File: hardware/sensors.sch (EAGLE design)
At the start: 30 parts, among them J1 CDH, J2 OW, J3 DBG, J4 SUN-UART, J5 ADCS, J6 ENV, J7 SUN, U1 DS18B20, U2 DS18B20, U3 DS18B20

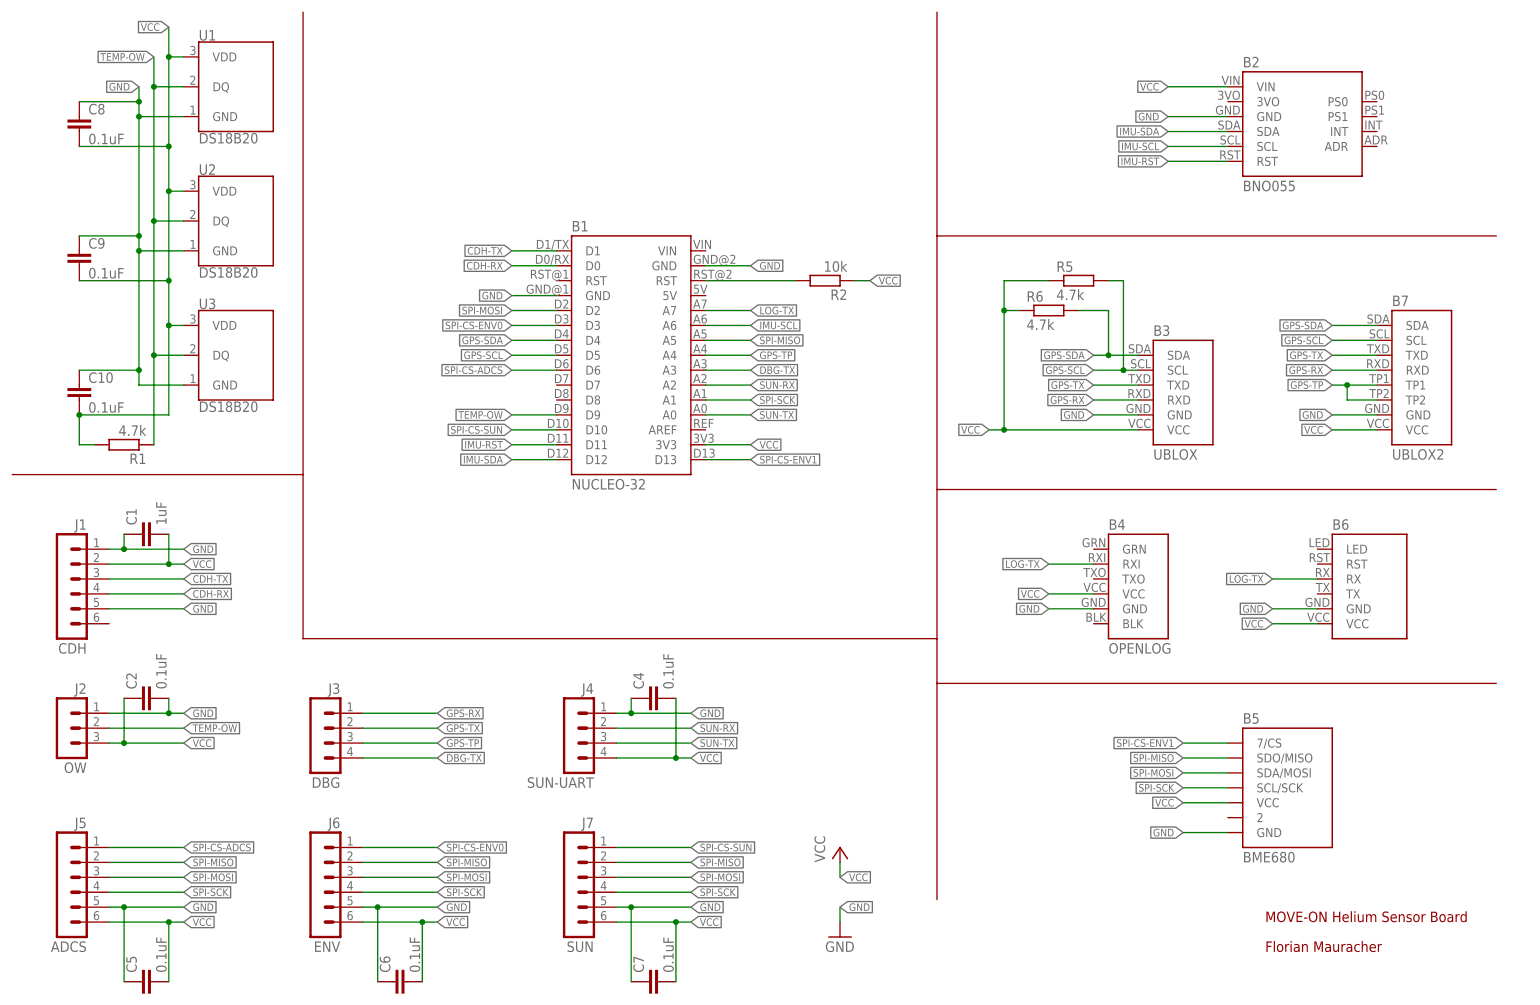
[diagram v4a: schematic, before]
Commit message: Update component names
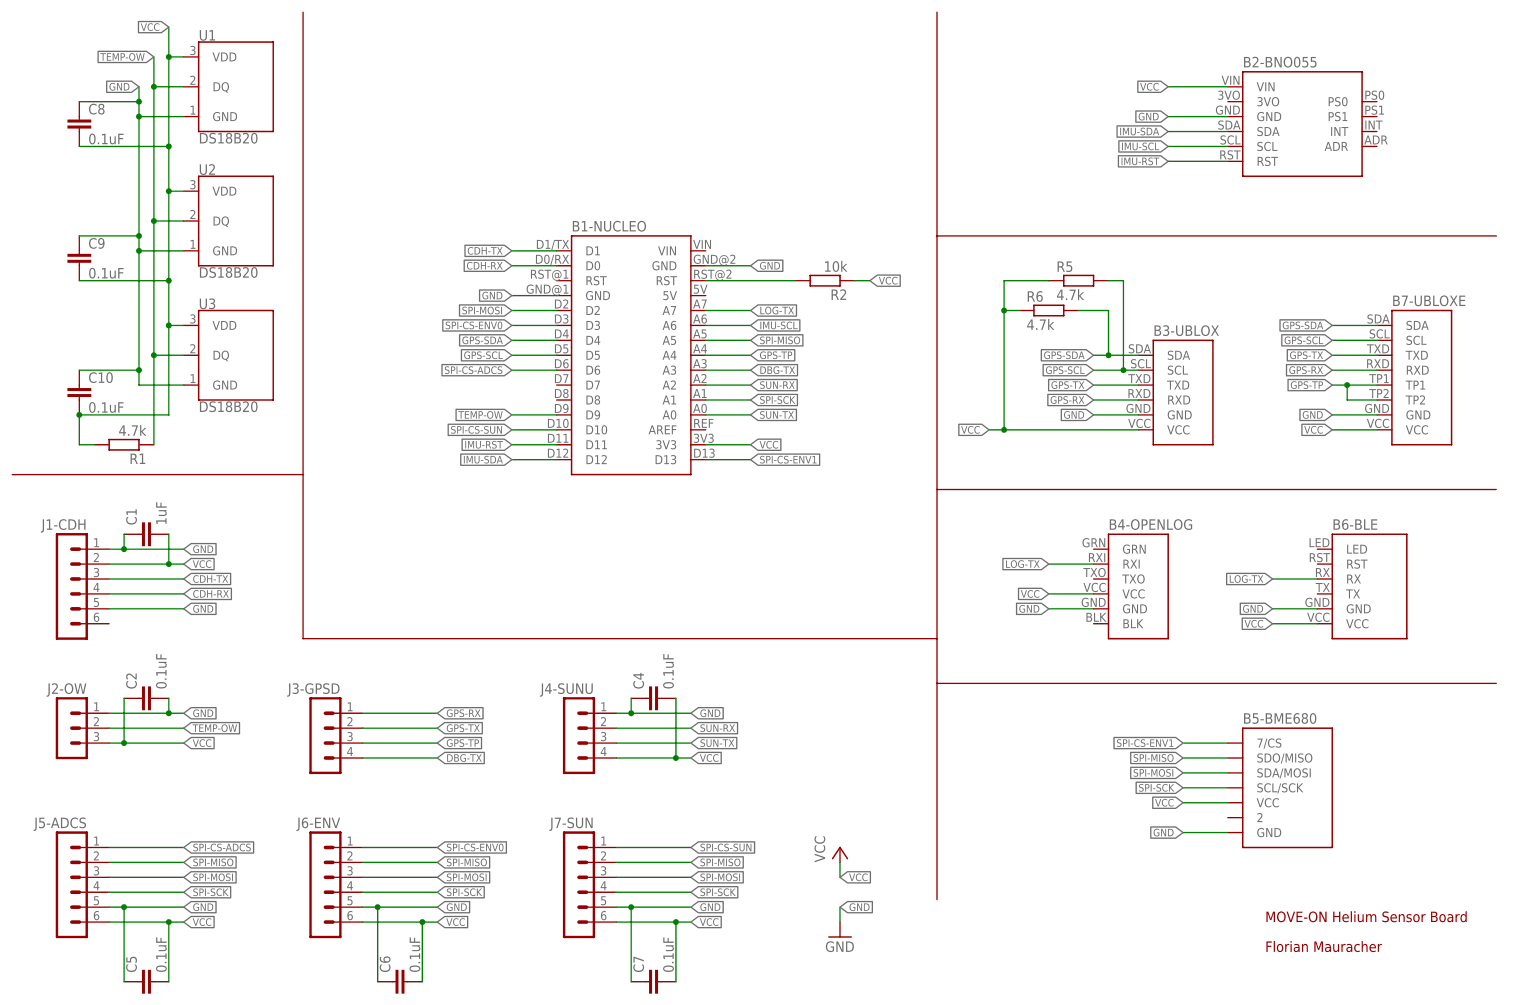
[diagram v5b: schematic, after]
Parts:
- B1-NUCLEO: value NUCLEO-32 -> (none)
- B2-BNO055: value BNO055 -> (none)
- B3-UBLOX: value UBLOX -> (none)
- B4-OPENLOG: value OPENLOG -> (none)
- B5-BME680: value BME680 -> (none)
- B7-UBLOXE: value UBLOX2 -> UPUTRONICS-UBLOX-M8Q
- J1-CDH: value CDH -> 90136-106
- J2-OW: value OW -> 90136-103
- J3-GPSD: value DBG -> 90136-104
- J4-SUNU: value SUN-UART -> 90136-104
- J5-ADCS: value ADCS -> 90136-106
- J6-ENV: value ENV -> 90136-106
- J7-SUN: value SUN -> 90136-106
- renumbered B1 to B1-NUCLEO, B2 to B2-BNO055, B3 to B3-UBLOX, B4 to B4-OPENLOG, B5 to B5-BME680, B6 to B6-BLE, B7 to B7-UBLOXE, J1 to J1-CDH, J2 to J2-OW, J3 to J3-GPSD, J4 to J4-SUNU, J5 to J5-ADCS, J6 to J6-ENV, J7 to J7-SUN

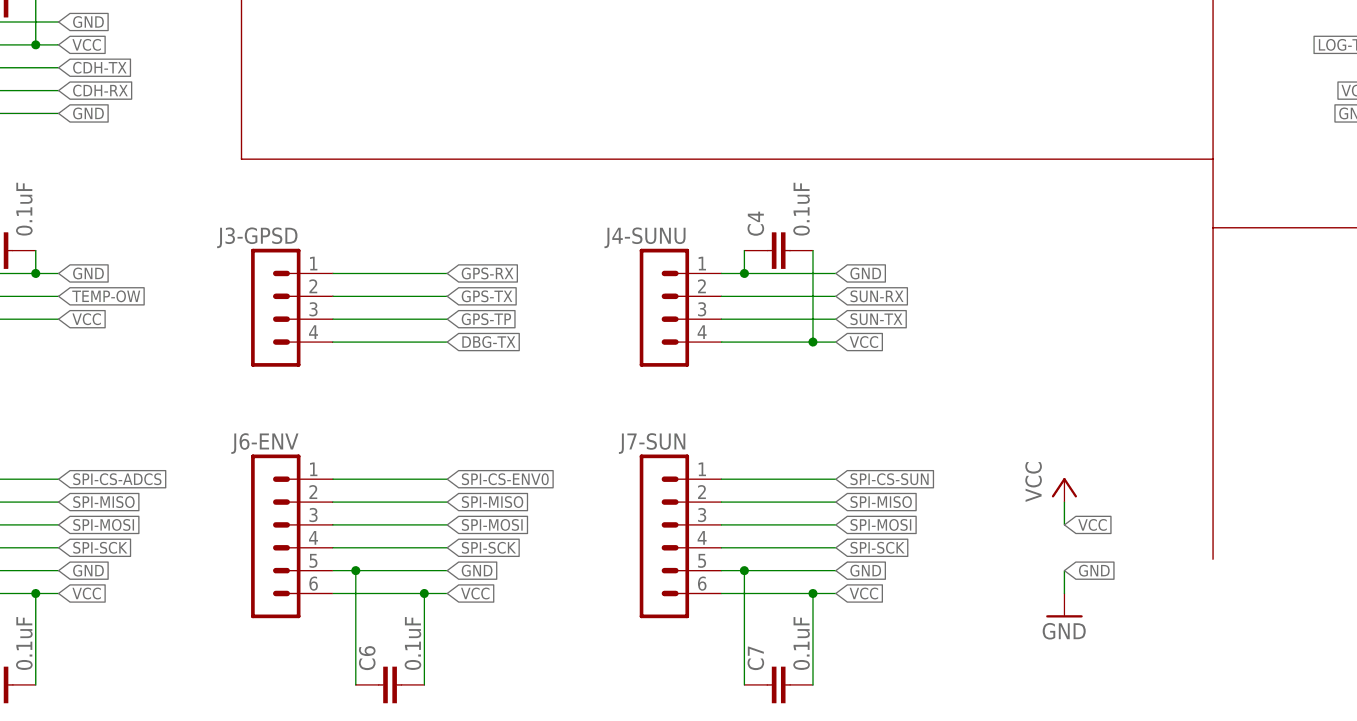
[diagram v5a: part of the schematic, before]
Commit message: Add I2C connector
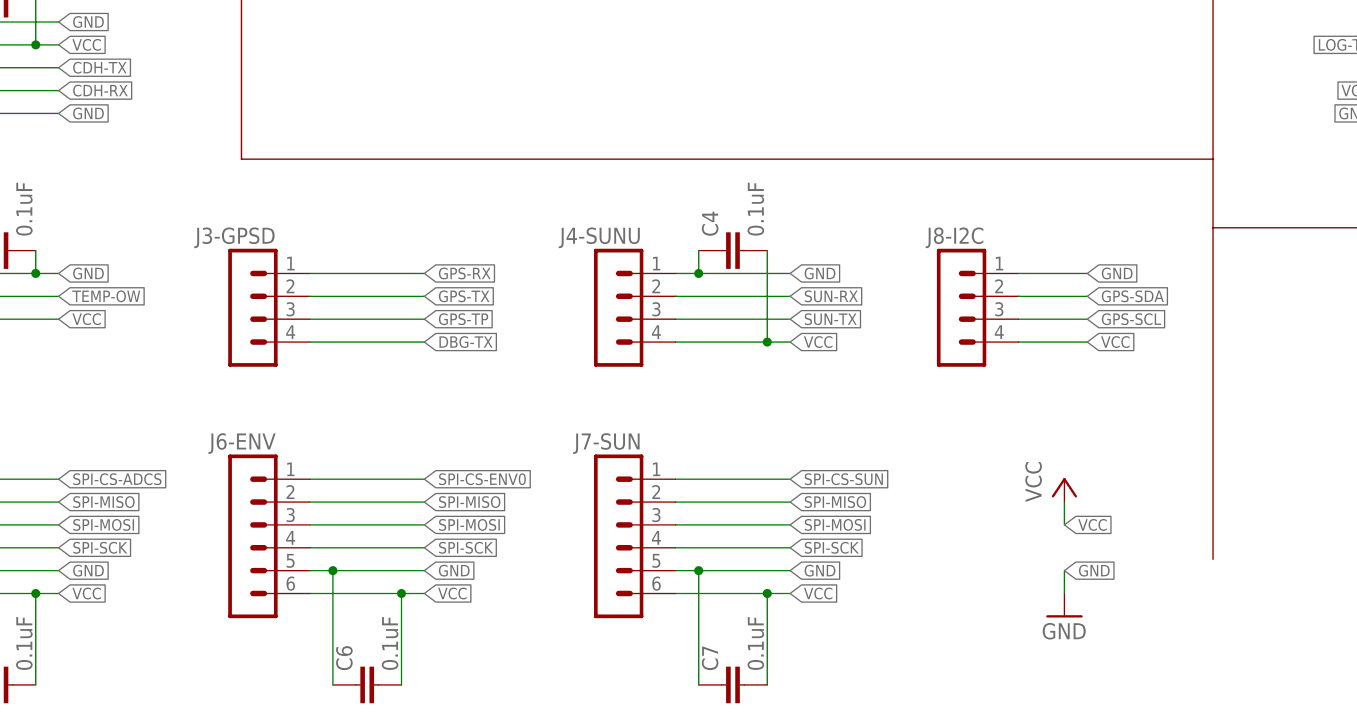
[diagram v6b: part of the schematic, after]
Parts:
- added J8-I2C: 90136-104, con-molex-c-grid:90136-104
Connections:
- net GND: now also J8-I2C.1
- net GPS-SCL: now also J8-I2C.3
- net GPS-SDA: now also J8-I2C.2
- net VCC: now also J8-I2C.4
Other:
- moved on the sheet: C4, C6, C7, J3-GPSD, J4-SUNU, J6-ENV, J7-SUN

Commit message: Add cap for I2C connector
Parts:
- added C3: 0.1uF, rcl:C-EUC2012
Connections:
- net GND: now also C3.1
- net VCC: now also C3.2
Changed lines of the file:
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@@
 <setting verticaltext="up"/>
 </settings>
-<grid distance="0.1" unitdist="inch" unit="inch" style="lines" multiple="1" display="yes" altdistance="0.01" altunitdist="inch" altunit="inch"/>
+<grid distance="0.1" unitdist="inch" unit="inch" style="lines" multiple="1" display="no" altdistance="0.01" altunitdist="inch" altunit="inch"/>
 <layers>
 <layer number="1" name="Top" color="4" fill="1" visible="no" active="no"/>
@@
 <part name="B7-UBLOXE" library="Frcy" deviceset="UPUTRONICS-UBLOX-M8Q" device="" value=""/>
 <part name="J8-I2C" library="con-molex-c-grid" deviceset="90136-1?04" device="" value=""/>
+<part name="C3" library="rcl" library_urn="urn:adsk.eagle:library:334" deviceset="C-EU" device="C2012" package3d_urn="urn:adsk.eagle:package:23625/2" value="0.1uF"/>
 </parts>
 <sheets>
@@
 <instance part="B7-UBLOXE" gate="G$1" x="241.3" y="114.3"/>
 <instance part="J8-I2C" gate="G$1" x="134.62" y="53.34" rot="MR0"/>
+<instance part="C3" gate="G$1" x="142.24" y="40.64" rot="R90"/>
 </instances>
 <busses>
@@
 <wire x1="139.7" y1="48.26" x2="147.32" y2="48.26" width="0.1524" layer="91"/>
 <label x="147.32" y="48.26" size="1.27" layer="95" xref="yes"/>
+<pinref part="C3" gate="G$1" pin="2"/>
+<wire x1="147.32" y1="40.64" x2="147.32" y2="48.26" width="0.1524" layer="91"/>
 </segment>
 </net>
@@
 <wire x1="139.7" y1="55.88" x2="147.32" y2="55.88" width="0.1524" layer="91"/>
 <label x="147.32" y="55.88" size="1.27" layer="95" xref="yes"/>
+<pinref part="C3" gate="G$1" pin="1"/>
+<wire x1="139.7" y1="55.88" x2="139.7" y2="40.64" width="0.1524" layer="91"/>
+<junction x="139.7" y="55.88"/>
 </segment>
 </net>
